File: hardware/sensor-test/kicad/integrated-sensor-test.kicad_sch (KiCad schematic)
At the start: 34 parts, among them J1 Conn_02x18_Odd_Even, J2 Conn_01x02, J3 USB_B_Micro, J4 Conn_02x18_Odd_Even, U1 NCP1117-3.3_SOT223, U2 W25Q128JVS, U3 RP2040, Y1 ABLS-12.000MHZ-B4-T

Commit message: Normalize integrated schematic reference designators
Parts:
- renumbered C1 to C17, C2 to C90, C17 to C91, J3 to J90, J1 to J91, J4 to J92, J2 to J93, R1 to R8, R2 to R9, U3 to U1, U1 to U90

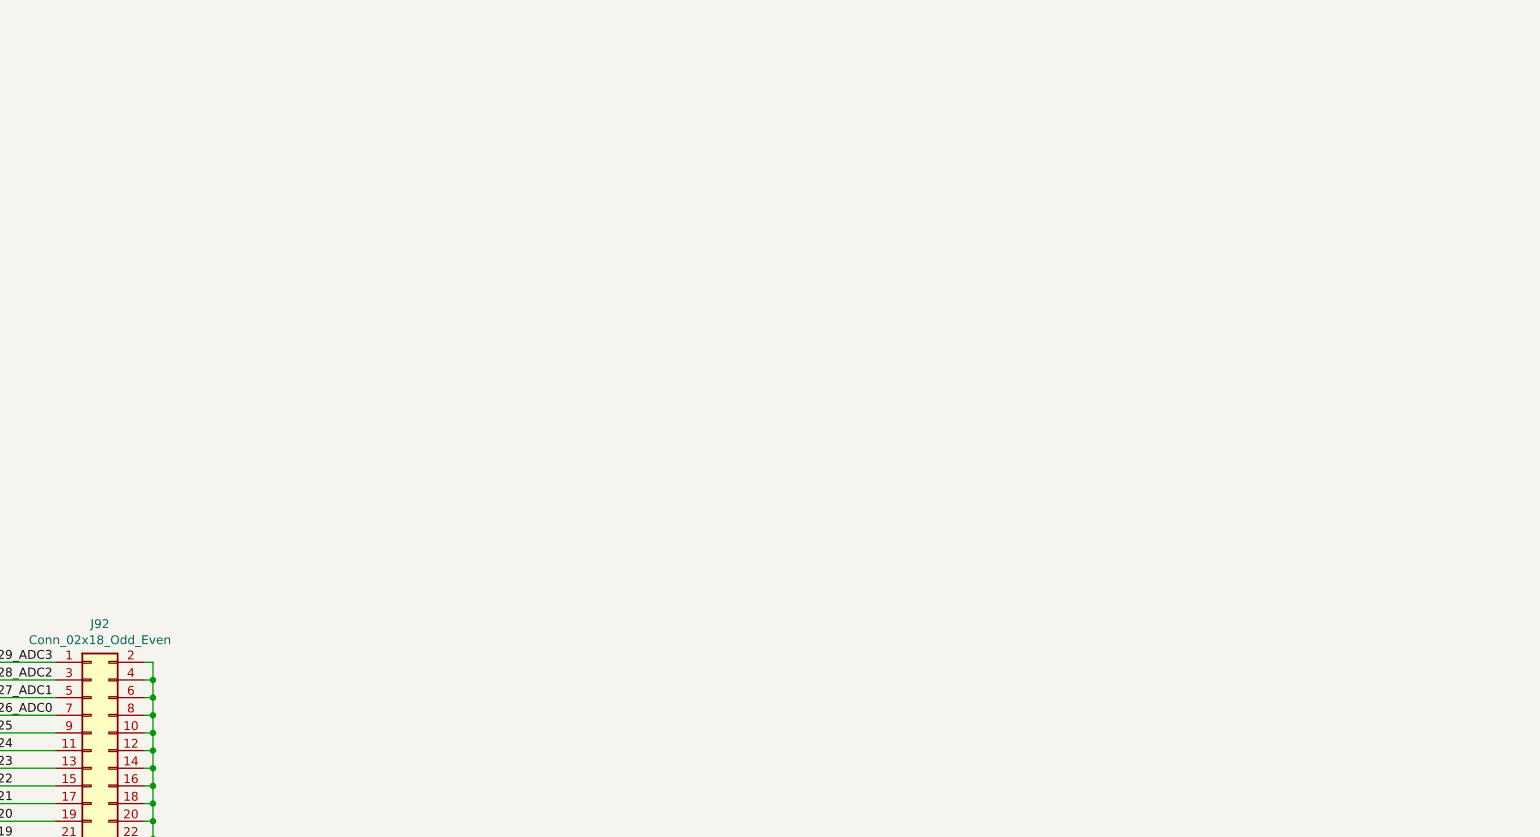
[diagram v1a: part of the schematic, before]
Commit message: Add isolated USB power block to integrated schematic
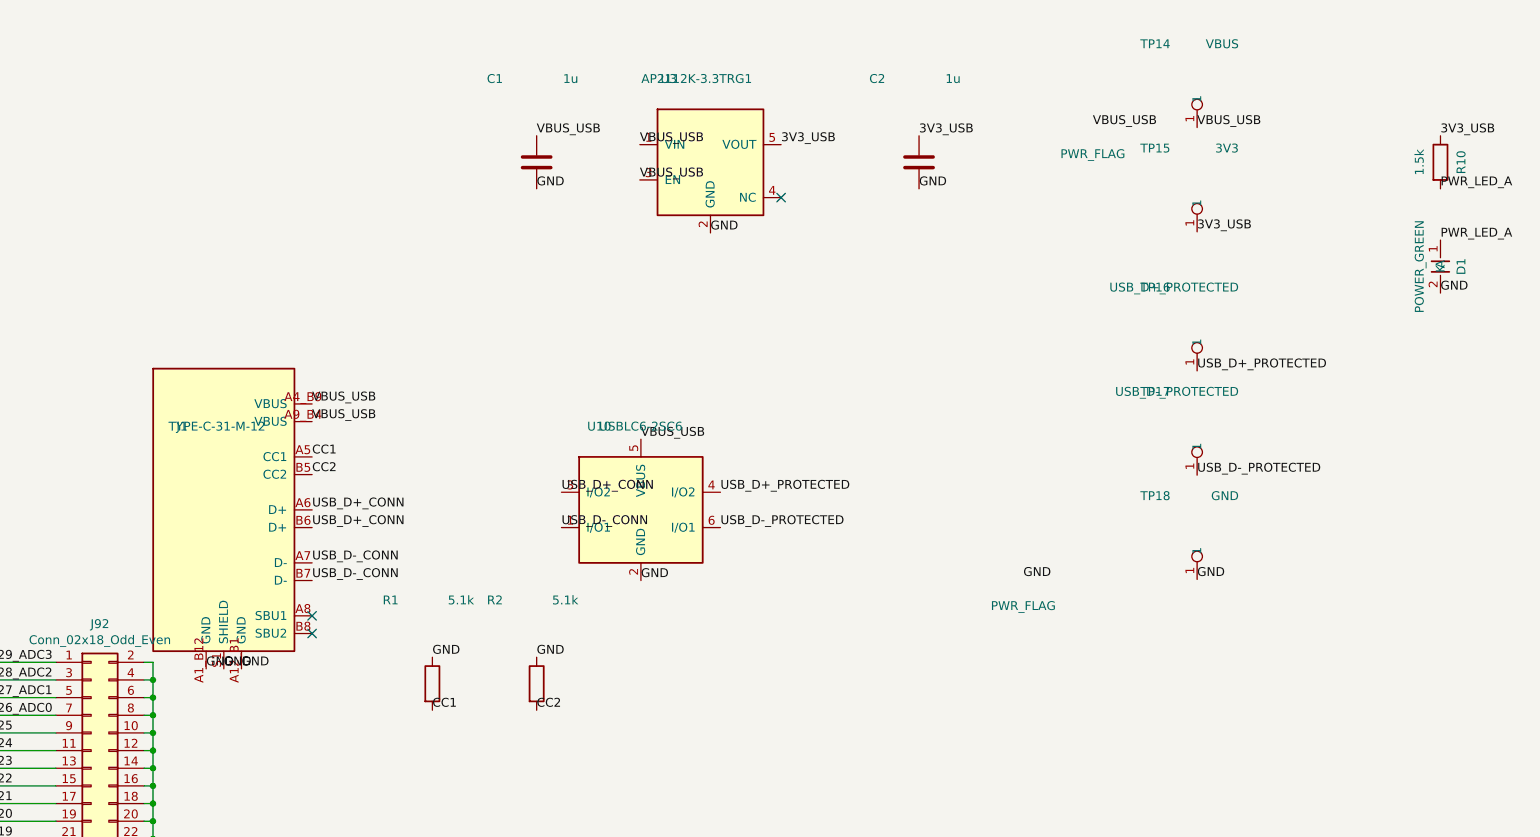
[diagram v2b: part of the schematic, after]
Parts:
- added C1, C2: 1u, Capacitor_SMD:C_0603_1608Metric, symbol Device:C
- added D1: POWER_GREEN, LED_SMD:LED_0603_1608Metric, symbol HEP:LED
- added J1: TYPE-C-31-M-12, Connector_USB:USB_C_Receptacle_HRO_TYPE-C-31-M-12, symbol HEP:HRO_TYPE-C-31-M-12
- added R1, R2: 5.1k, Resistor_SMD:R_0603_1608Metric, symbol Device:R
- added R10: 1.5k, Resistor_SMD:R_0603_1608Metric, symbol Device:R
- added TP14: VBUS, TestPoint:TestPoint_Pad_D1.5mm, symbol Connector:TestPoint
- added TP15: 3V3, TestPoint:TestPoint_Pad_D1.5mm, symbol Connector:TestPoint
- added TP16: USB_D+_PROTECTED, TestPoint:TestPoint_Pad_D1.5mm, symbol Connector:TestPoint
- added TP17: USB_D-_PROTECTED, TestPoint:TestPoint_Pad_D1.5mm, symbol Connector:TestPoint
- added TP18: GND, TestPoint:TestPoint_Pad_D1.5mm, symbol Connector:TestPoint
- added U10: USBLC6-2SC6, Package_TO_SOT_SMD:SOT-23-6, symbol HEP:USBLC6-2SC6
- added U3: AP2112K-3.3TRG1, Package_TO_SOT_SMD:SOT-23-5, symbol HEP:AP2112K-3.3
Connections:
- net GND: now also C1.2, C2.2, D1.2 (A), J1.A12_B1 (GND), J1.A1_B12 (GND), J1.S1 (SHIELD), R1.1, R2.1, TP18.1, U10.2 (GND), U3.2 (GND)
- new net 3V3_USB: C2.1, R10.1, TP15.1, U3.5 (VOUT)
- new net CC1: J1.A5 (CC1), R1.2
- new net CC2: J1.B5 (CC2), R2.2
- new net PWR_LED_A: D1.1 (K), R10.2
- new net USB_D+_CONN: J1.A6 (D+), J1.B6 (D+), U10.3 (I/O2)
- new net USB_D+_PROTECTED: TP16.1, U10.4 (I/O2)
- new net USB_D-_CONN: J1.A7 (D-), J1.B7 (D-), U10.1 (I/O1)
- new net USB_D-_PROTECTED: TP17.1, U10.6 (I/O1)
- new net VBUS_USB: C1.1, J1.A4_B9 (VBUS), J1.A9_B4 (VBUS), TP14.1, U10.5 (VBUS), U3.1 (VIN), U3.3 (EN)
- no-connect marks 1 -> 4

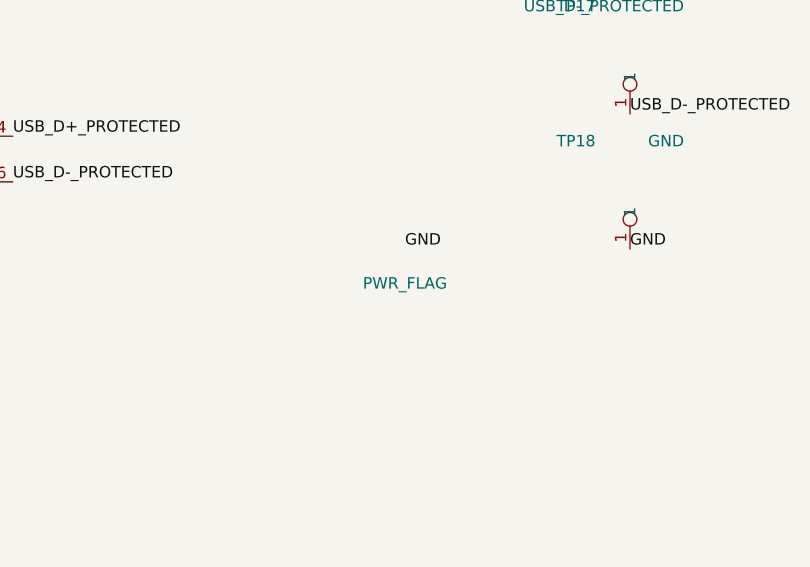
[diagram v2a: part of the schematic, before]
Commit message: Remove redundant integrated GND power flag
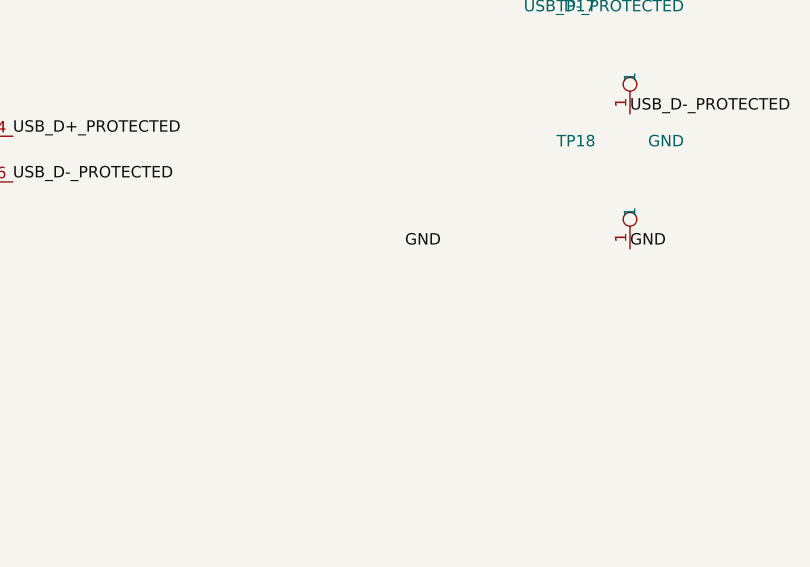
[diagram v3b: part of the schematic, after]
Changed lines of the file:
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@@
     )
   (label "GND" (at 535 110 0) (effects (font (size 1.27 1.27)) (justify left bottom)))
-  (symbol (lib_id "power:PWR_FLAG") (at 510 110 0) (unit 1)
-      (in_bom yes) (on_board yes) (dnp no)
-      (property "Reference" "#FLG01" (at 510 111.905 0) (effects (font (size 1.27 1.27)) hide))
-      (property "Value" "PWR_FLAG" (at 510 113.81 0) (effects (font (size 1.27 1.27))))
-      (property "Footprint" "" (at 510 110 0) (effects (font (size 1.27 1.27)) hide))
-      (property "Datasheet" "~" (at 510 110 0) (effects (font (size 1.27 1.27)) hide))
-      (pin "1")
-      (instances
-        (project "integrated-sensor-test"
-          (path "/0b572f4d-42c2-4e67-a259-3bf815f1855a"
-            (reference "#FLG01") (unit 1)
-          )
-        )
-      )
-    )
   (label "GND" (at 510 110 0)
       (effects (font (size 1.27 1.27)) (justify left bottom))
